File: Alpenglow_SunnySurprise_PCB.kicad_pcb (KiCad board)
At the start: 2 copper layers, 52.4 x 52.4 mm, 9 parts, among them SW1 SW_SPDT

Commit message: Updated board name font, updated @alpenglowind with oswald font
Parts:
- added G***: LOGO, Alpenglow:@AlpenglowIndOswald20mm, B.Cu at (152.7, 78.4)
- added G***: LOGO, Alpenglow_Sun_PCB:SUS board name font 20x3.7mm, B.Cu at (152.9, 111.0)
- moved G*** 4.27 mm to (153.3, 104.5)
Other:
- board text added: "+ LONG - SHORT"
- board text removed: "@AlpenglowInd"
- board text removed: "LONG"
- board text removed: "SHORT"
- board text removed: "SUNNY SURPRISE!"

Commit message: Updated switch footprint
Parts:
- SW1: footprint Alpenglow:SW_SLIDE_RTA -> Alpenglow:SW_SPDT_SLIDE_THRU_RTA
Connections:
- SW1 pad : GND -> (no net)

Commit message: Updated Switch, Removed GND pour and added GND traces, Updated artwork
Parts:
- removed the G*** at (152.5, 91.0)
- added ? (x4): , Graphics, F.Cu at (146.2, -38.4)
- added ?: , Graphics, B.Cu at (145.8, 94.1)
- added ?: , Graphics, B.Cu at (146.2, -38.4)
- added ? (x4): , Graphics, F.Cu at (145.8, 94.1)
- added ?: , Graphics, F.Cu at (133.2, 51.9)
- SW1: footprint Alpenglow:SW_SPDT_SLIDE_THRU_RTA -> Alpenglow:Alpenglow_SW_SPDT_3pin_RTA
- moved SW1 14.2 mm to (177.4, 70.2), turned to 150 degrees
- moved D3 14.1 mm to (184.5, 71.2)
- moved G*** 14.1 mm to (164.0, 95.4)
- moved G*** 14.1 mm to (163.3, 69.3)
- moved G*** 14.1 mm to (163.6, 101.9)
- moved D1 14.1 mm to (164.6, 57.4)
- moved D2 14.1 mm to (143.0, 70.0)
- moved D4 14.1 mm to (144.8, 94.7)
- moved BT1 14.1 mm to (152.5, 80.3)
- moved D5 13.2 mm to (180.3, 96.1), turned to 51 degrees
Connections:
- SW1 pad 1: Net-(SW1-Pad1) -> unconnected-(SW1-Pad1)
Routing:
- net GND: track 0.00 -> 148.8 mm, vias 0 -> 8
- net VCC: track 51.4 -> 44.1 mm
- net Net-(D1-Pad2): track 111.4 -> 107.1 mm
- added copper zone on B.Cu, net (none)
- added copper zone on F.Cu, net (none)
- removed copper zone on B.Cu, net GND
- removed copper zone on F.Cu, net GND

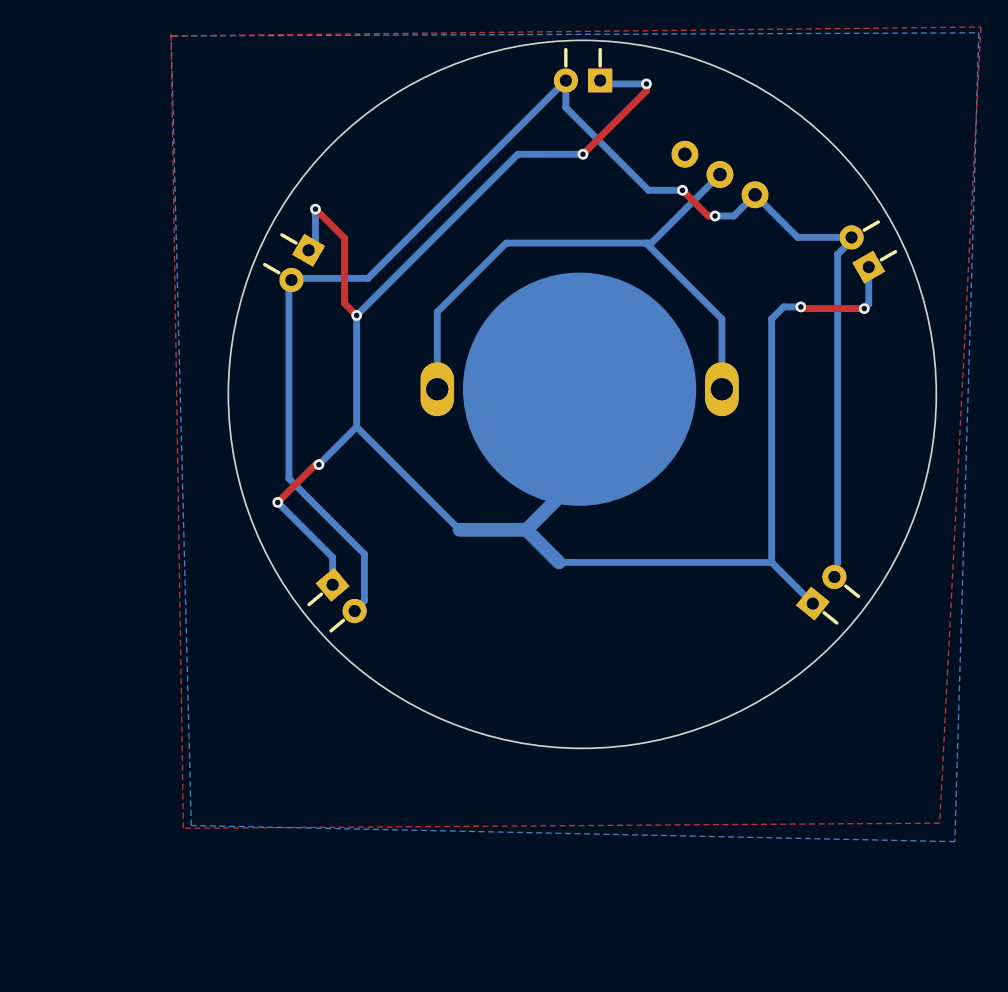
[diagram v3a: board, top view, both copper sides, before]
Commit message: cleaned up some traces and text
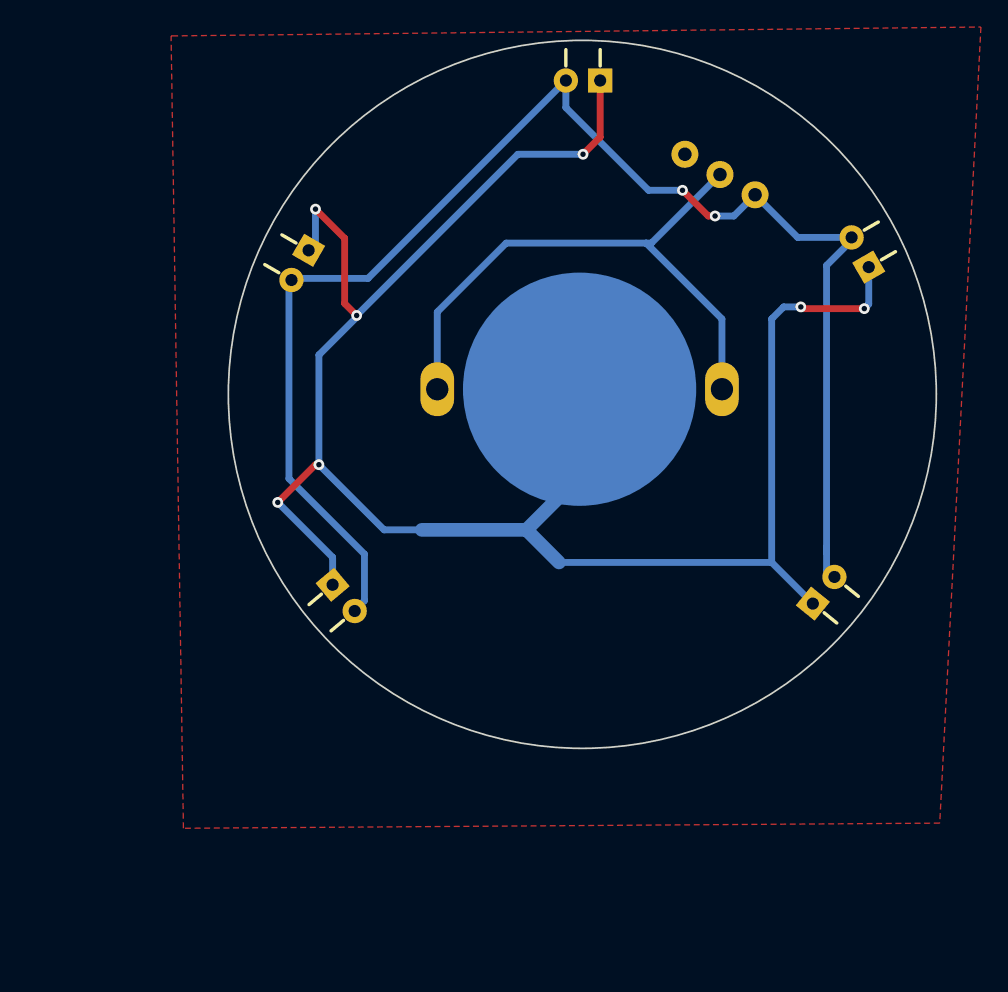
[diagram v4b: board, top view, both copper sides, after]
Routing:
- net GND: track 148.8 -> 146.0 mm, vias 8 -> 7
- net Net-(D1-Pad2): track 107.1 -> 109.1 mm
- removed copper zone on B.Cu, net (none)
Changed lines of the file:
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@@
     (property "Sheetname" "")
     (attr through_hole)
-    (fp_text reference "BT1" (at 0 11.176) (layer "B.SilkS") hide
+    (fp_text reference "BT1" (at -0.635 -9.144) (layer "B.SilkS")
       (effects (font (size 1 1) (thickness 0.15)) (justify mirror))
     )
-    (fp_text value "Battery_Cell" (at -6.096 17.018) (layer "B.Fab")
+    (fp_text value "Battery_Cell" (at -6.096 17.018) (layer "B.Fab") hide
       (effects (font (size 1 1) (thickness 0.15)) (justify mirror))
     )
@@
     (property "Sheetname" "")
     (attr through_hole)
-    (fp_text reference "SW1" (at -4.3 0.7 330 unlocked) (layer "B.SilkS")
+    (fp_text reference "SW1" (at 12.665456 2.477293 unlocked) (layer "B.SilkS")
       (effects (font (size 1 1) (thickness 0.15)) (justify mirror))
     )
-    (fp_text value "SW_SPDT" (at 0 -1 330 unlocked) (layer "B.Fab")
+    (fp_text value "SW_SPDT" (at 0 -1 330 unlocked) (layer "B.Fab") hide
       (effects (font (size 1 1) (thickness 0.15)) (justify mirror))
     )
@@
     (effects (font (size 1 1) (thickness 0.15)) (justify mirror))
   )
-  (gr_text "OFF" (at 169.926 57.8358 60) (layer "B.SilkS")
+  (gr_text "OFF" (at 169.418 57.15 60) (layer "B.SilkS")
     (effects (font (size 1 1) (thickness 0.15)) (justify mirror))
   )
@@
     (effects (font (size 1.27 1.27) (thickness 0.1524)) (justify right mirror))
   )
+  (segment (start 163.322 62.865) (end 164.592 61.595) (width 0.508) (layer "F.Cu") (net 1))
   (segment (start 179.578 74.295) (end 179.451 74.168) (width 0.508) (layer "F.Cu") (net 1))
   (segment (start 143.51 85.852) (end 140.716 88.646) (width 0.508) (layer "F.Cu") (net 1))
   (segment (start 145.669 73.914) (end 146.558 74.803) (width 0.508) (layer "F.Cu") (net 1))
-  (segment (start 168.021 58.166) (end 163.322 62.865) (width 0.508) (layer "F.Cu") (net 1))
   (segment (start 145.669 69.088) (end 145.669 73.914) (width 0.508) (layer "F.Cu") (net 1))
   (segment (start 184.15 74.295) (end 179.578 74.295) (width 0.508) (layer "F.Cu") (net 1))
   (segment (start 143.764 85.852) (end 143.51 85.852) (width 0.508) (layer "F.Cu") (net 1))
+  (segment (start 164.592 61.595) (end 164.592 57.404) (width 0.508) (layer "F.Cu") (net 1))
   (segment (start 143.51 66.929) (end 145.669 69.088) (width 0.508) (layer "F.Cu") (net 1))
-  (segment (start 168.021 57.658) (end 168.021 58.166) (width 0.508) (layer "F.Cu") (net 1))
   (via (at 184.15 74.295) (size 0.8) (drill 0.4) (layers "F.Cu" "B.Cu") (net 1))
   (via (at 143.764 85.852) (size 0.8) (drill 0.4) (layers "F.Cu" "B.Cu") (net 1))
@@
   (via (at 146.558 74.803) (size 0.8) (drill 0.4) (layers "F.Cu" "B.Cu") (net 1))
   (via (at 140.716 88.646) (size 0.8) (drill 0.4) (layers "F.Cu" "B.Cu") (net 1))
-  (via (at 168.021 57.658) (size 0.8) (drill 0.4) (layers "F.Cu" "B.Cu") (net 1))
   (via (at 179.451 74.168) (size 0.8) (drill 0.4) (layers "F.Cu" "B.Cu") (net 1))
   (segment (start 177.292 93.091) (end 180.34 96.139) (width 0.508) (layer "B.Cu") (net 1))
-  (segment (start 164.846 57.658) (end 164.592 57.404) (width 0.508) (layer "B.Cu") (net 1))
-  (segment (start 146.558 83.058) (end 143.764 85.852) (width 0.508) (layer "B.Cu") (net 1))
-  (segment (start 168.021 57.658) (end 164.846 57.658) (width 0.508) (layer "B.Cu") (net 1))
+  (segment (start 148.59 90.678) (end 143.764 85.852) (width 0.508) (layer "B.Cu") (net 1))
   (segment (start 159.131 90.678) (end 163.068 86.741) (width 1.016) (layer "B.Cu") (net 1))
+  (segment (start 164.846 57.658) (end 164.592 57.404) (width 0.508) (layer "B.Cu") (net 1))
   (segment (start 143.51 66.929) (end 143.51 69.469) (width 0.508) (layer "B.Cu") (net 1))
   (segment (start 161.544 93.091) (end 159.131 90.678) (width 1.016) (layer "B.Cu") (net 1))
-  (segment (start 146.558 83.058) (end 154.178 90.678) (width 0.508) (layer "B.Cu") (net 1))
+  (segment (start 151.384 90.678) (end 159.131 90.678) (width 1.016) (layer "B.Cu") (net 1))
   (segment (start 179.451 74.168) (end 178.181 74.168) (width 0.508) (layer "B.Cu") (net 1))
   (segment (start 177.292 93.091) (end 161.544 93.091) (width 0.508) (layer "B.Cu") (net 1))
+  (segment (start 146.558 74.803) (end 146.558 74.93) (width 0.508) (layer "B.Cu") (net 1))
   (segment (start 163.068 86.741) (end 163.068 80.264) (width 1.016) (layer "B.Cu") (net 1))
   (segment (start 144.78 92.71) (end 144.78 94.742) (width 0.508) (layer "B.Cu") (net 1))
-  (segment (start 154.178 90.678) (end 159.131 90.678) (width 1.016) (layer "B.Cu") (net 1))
+  (segment (start 151.384 90.678) (end 148.59 90.678) (width 0.508) (layer "B.Cu") (net 1))
   (segment (start 158.496 62.865) (end 146.558 74.803) (width 0.508) (layer "B.Cu") (net 1))
   (segment (start 184.4802 71.2216) (end 184.4802 73.9648) (width 0.508) (layer "B.Cu") (net 1))
-  (segment (start 146.558 74.803) (end 146.558 83.058) (width 0.508) (layer "B.Cu") (net 1))
+  (segment (start 146.558 74.93) (end 143.764 77.724) (width 0.508) (layer "B.Cu") (net 1))
   (segment (start 140.716 88.646) (end 144.78 92.71) (width 0.508) (layer "B.Cu") (net 1))
   (segment (start 184.4802 73.9648) (end 184.15 74.295) (width 0.508) (layer "B.Cu") (net 1))
   (segment (start 178.181 74.168) (end 177.292 75.057) (width 0.508) (layer "B.Cu") (net 1))
   (segment (start 163.322 62.865) (end 158.496 62.865) (width 0.508) (layer "B.Cu") (net 1))
+  (segment (start 143.764 77.724) (end 143.764 85.852) (width 0.508) (layer "B.Cu") (net 1))
   (segment (start 177.292 75.057) (end 177.292 93.091) (width 0.508) (layer "B.Cu") (net 1))
   (segment (start 143.51 69.469) (end 143.002 69.977) (width 0.508) (layer "B.Cu") (net 1))
@@
   (segment (start 141.545116 86.884316) (end 147.136883 92.476083) (width 0.508) (layer "B.Cu") (net 3))
   (segment (start 174.490524 67.437) (end 176.062076 65.865448) (width 0.508) (layer "B.Cu") (net 3))
-  (segment (start 182.177884 70.275682) (end 183.406319 69.047247) (width 0.508) (layer "B.Cu") (net 3))
+  (segment (start 181.356 91.948) (end 181.356 93.726) (width 0.508) (layer "B.Cu") (net 3))
+  (segment (start 181.356 92.34747) (end 181.356 91.948) (width 0.508) (layer "B.Cu") (net 3))
   (segment (start 147.136883 95.922647) (end 146.236884 96.822646) (width 0.508) (layer "B.Cu") (net 3))
+  (segment (start 181.356 93.726) (end 181.864 94.234) (width 0.508) (layer "B.Cu") (net 3))
   (segment (start 147.398354 72.057646) (end 162.052 57.404) (width 0.508) (layer "B.Cu") (net 3))
   (segment (start 141.545116 72.057646) (end 141.545116 86.884316) (width 0.508) (layer "B.Cu") (net 3))
@@
   (segment (start 179.218523 69.021895) (end 183.2102 69.021895) (width 0.508) (layer "B.Cu") (net 3))
   (segment (start 141.545116 72.057646) (end 147.398354 72.057646) (width 0.508) (layer "B.Cu") (net 3))
+  (segment (start 181.356 91.948) (end 181.356 71.097566) (width 0.508) (layer "B.Cu") (net 3))
+  (segment (start 181.356 71.097566) (end 183.406319 69.047247) (width 0.508) (layer "B.Cu") (net 3))
   (segment (start 147.136883 92.476083) (end 147.136883 95.922647) (width 0.508) (layer "B.Cu") (net 3))
   (segment (start 162.052 59.4106) (end 162.052 57.404) (width 0.508) (layer "B.Cu") (net 3))
-  (segment (start 182.177884 93.169354) (end 182.177884 70.275682) (width 0.508) (layer "B.Cu") (net 3))
   (zone (net 0) (net_name "") (layer "F.Cu") (hatch edge 0.508)
     (connect_pads (clearance 0.508))
@@
       )
     )
-  )
-  (zone (net 0) (net_name "") (layer "B.Cu") (hatch edge 0.508)
-    (connect_pads (clearance 0.508))
-    (min_thickness 0.254) (filled_areas_thickness no)
-    (fill yes (thermal_gap 0.508) (thermal_bridge_width 0.508))
-    (polygon
-      (pts
-        (xy 190.8556 113.7666)
-        (xy 134.3152 112.5728)
-        (xy 132.8166 54.0004)
-        (xy 132.8928 54.102)
-        (xy 192.6336 53.8734)
-      )
-    )

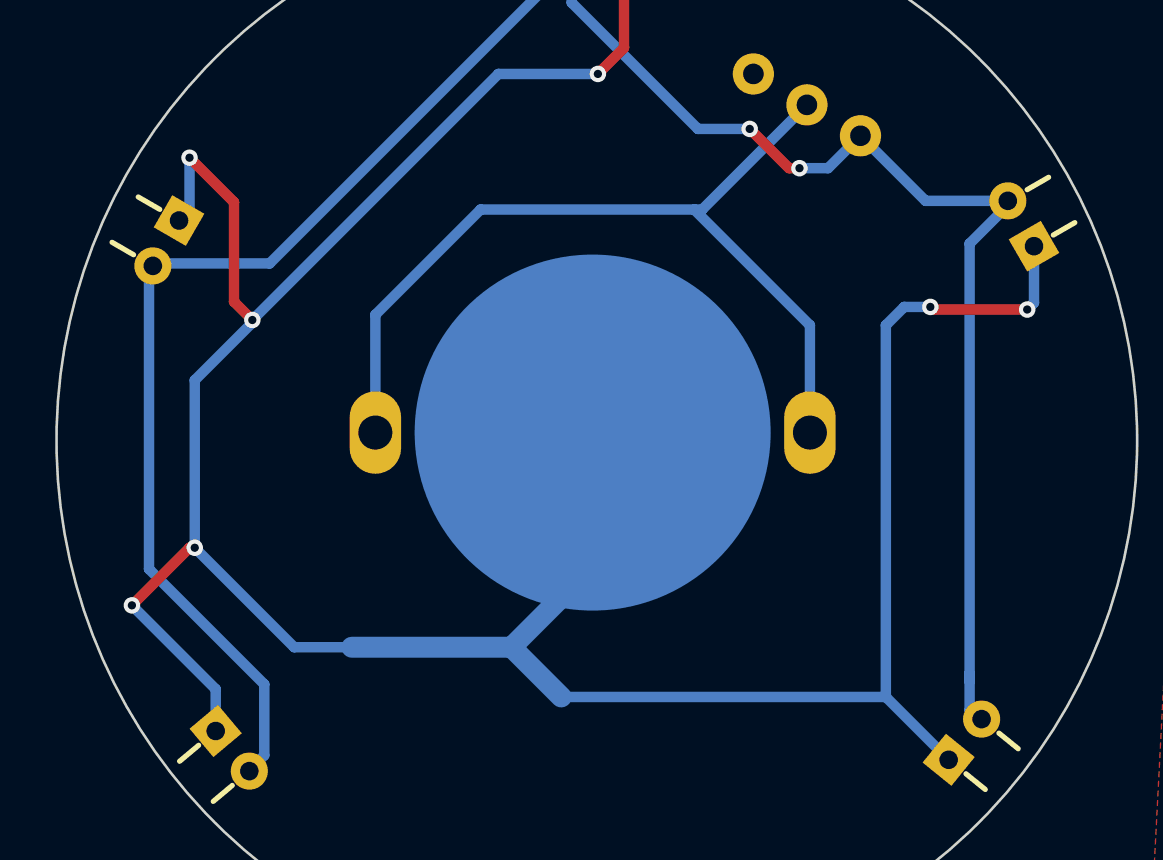
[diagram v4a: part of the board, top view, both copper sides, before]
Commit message: Updated font, Removed extra vias for GND traces, Renamed pwr net to LED+
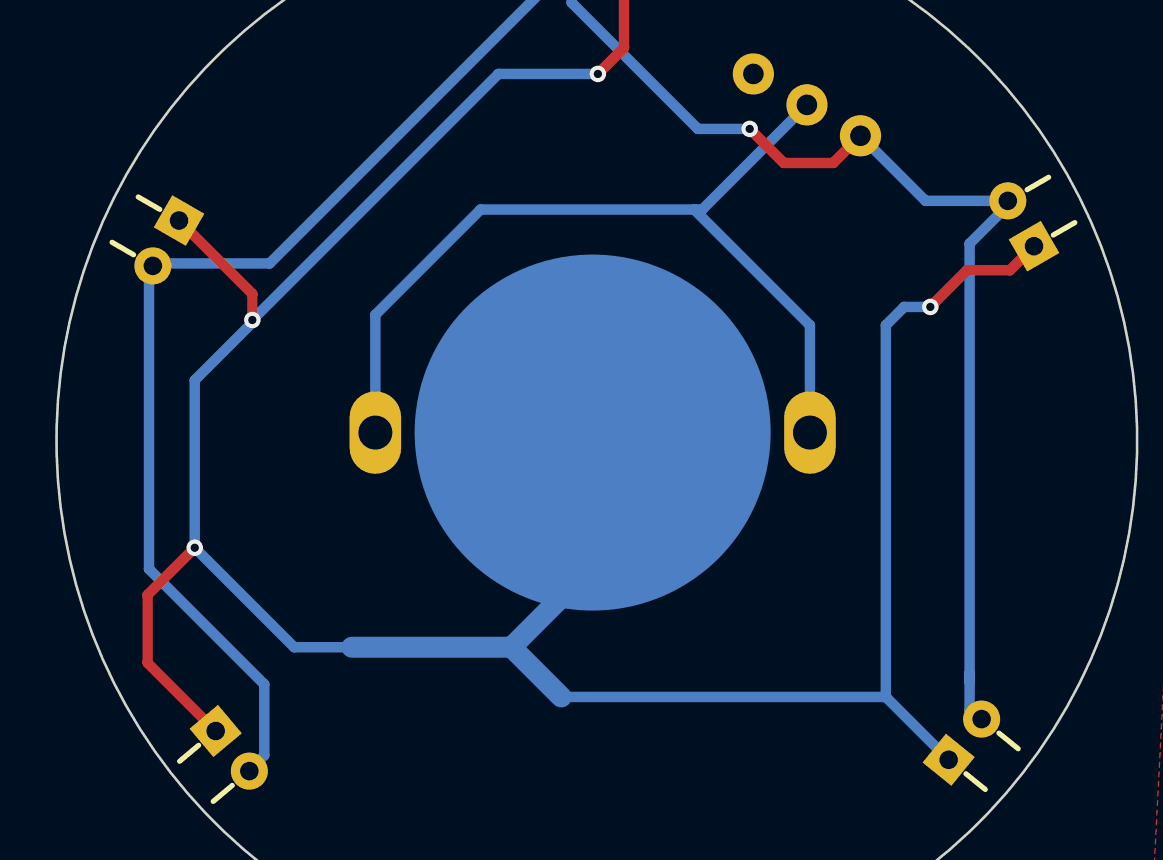
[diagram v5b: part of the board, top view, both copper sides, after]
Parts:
- removed the G*** at (163.3, 69.3)
- removed the G*** at (163.6, 101.9)
- added ? (x4): , Graphics, F.Cu at (189.1, 122.4)
- added ?: , Graphics, B.Cu at (211.1, 16.7)
- added ?: , Graphics, B.Cu at (164.5, 101.5)
- added ?: , Graphics, B.Cu at (189.1, 122.4)
- moved G*** 0.57 mm to (163.4, 95.1)
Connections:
- net Net-(D1-Pad2) renamed /LED+
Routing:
- net GND: track 146.0 -> 137.5 mm, vias 7 -> 4
- net /LED+: track 109.1 -> 108.9 mm, vias 2 -> 1

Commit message: cleaned up short tracks, added fab notes, generated gerbers
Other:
- board text added: "Sunny Surprise Rev 2.0 PCB Specifications: 1. 1 oz Cu, FR-4 2. 2 layers 3. 0.063 inch / 1.6mm thick 4. Soldermask: Yellow, both sides 5. Silkscreen: Red, both sides 6. Finish: ENIG"
